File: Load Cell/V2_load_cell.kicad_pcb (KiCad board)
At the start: 2 copper layers, 114.3 x 114.3 mm, 35 parts, among them J1 Conn_01x02, J10 Conn_01x06, J11 Conn_01x04, J12 Conn_01x06, J13 Conn_01x04, J14 Conn_01x06, J15 Conn_01x04, J16 Conn_01x06, J17 Conn_01x04, J2 Conn_01x06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

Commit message: 2-17-22
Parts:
- moved A1 18.4 mm to (74.9, 31.8)
- moved J1 18.4 mm to (81.3, 19.1)
- moved R4 12.7 mm to (38.7, 30.5), turned to 0 degrees
- moved R2 12.7 mm to (18.4, 30.5), turned to 0 degrees
- moved R6 12.7 mm to (18.4, 74.3), turned to 0 degrees
- moved R8 12.7 mm to (37.5, 74.3), turned to 0 degrees
- moved R5 8.64 mm to (18.4, 78.7), turned to 0 degrees
- moved R7 8.64 mm to (37.5, 78.7), turned to 0 degrees
- moved R1 7.96 mm to (18.4, 34.9), turned to 0 degrees
- moved R3 7.96 mm to (38.7, 34.9), turned to 0 degrees
- moved J11 2.54 mm to (21.0, 66.7)
- moved J13 2.54 mm to (41.3, 66.7)
- moved J10 2.54 mm to (31.1, 41.3)
- moved J12 2.54 mm to (51.4, 41.3)
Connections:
- J10 pad 3: /A+0 -> /Sheet61D3CBFB/A-
- J10 pad 4: /Sheet61D3CBFB/A- -> /A+0
- J11 pad 1: VCC -> GND
- J11 pad 4: GND -> VCC
- J12 pad 3: /A+1 -> /sheet61D4E250/A-
- J12 pad 4: /sheet61D4E250/A- -> /A+1
- J13 pad 1: VCC -> GND
- J13 pad 4: GND -> VCC
- J14 pad 3: /A+2 -> /sheet61D4EE5D/A-
- J14 pad 4: /sheet61D4EE5D/A- -> /A+2
- J15 pad 1: VCC -> GND
- J15 pad 4: GND -> VCC
- J16 pad 3: /A+3 -> /sheet61D4FC90/A-
- J16 pad 4: /sheet61D4FC90/A- -> /A+3
- J17 pad 1: VCC -> GND
- J17 pad 4: GND -> VCC
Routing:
- net VCC: track 207.8 -> 159.5 mm
- net /DT2: track 71.3 -> 97.0 mm
- net /SCK2: track 67.0 -> 91.5 mm
- net /A+1: track 69.2 -> 93.6 mm
- net /DT0: track 44.1 -> 67.3 mm
- net /SCK0: track 40.6 -> 62.2 mm
- net /DT1: track 21.7 -> 42.6 mm
- net /SCK1: track 18.1 -> 37.9 mm
- net /DT3: track 55.8 -> 73.2 mm
- net /SCK3: track 51.4 -> 68.2 mm
- net /A1: track 60.5 -> 75.7 mm
- net /TX1: track 57.1 -> 71.6 mm
- net /A+0: track 23.6 -> 34.6 mm
- net /E+2: track 40.0 -> 50.5 mm
- net /E+3: track 79.9 -> 90.4 mm
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- added copper zone on B.Cu, net GND

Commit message: pcb v2 update
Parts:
- J6, J7, J8, J9: footprint Connector_JST:JST_PH_B3B-PH-K_1x03_P2.00mm_Vertical -> Connector_JST:JST_PH_S3B-PH-K_1x03_P2.00mm_Horizontal
- moved J6 6.04 mm to (33.8, 19.7), turned to 180 degrees
- moved J7 4.02 mm to (109.9, 19.7), turned to 180 degrees
- moved H2 1.91 mm to (120.7, 19.1)
- moved J9 1.46 mm to (105.9, 119.4)
- moved J8 0.63 mm to (29.8, 119.4)
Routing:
- net VCC: track 159.5 -> 239.2 mm
- net /A+1: track 93.6 -> 77.6 mm
- net /E+1: track 67.0 -> 77.5 mm
- net /A+0: track 34.6 -> 41.5 mm
- net /E-0: track 24.5 -> 27.8 mm
- net /VIN: track 28.7 -> 26.8 mm
- net /E+3: track 90.4 -> 88.7 mm
- net /E+0: track 27.8 -> 29.3 mm
- net /E-3: track 86.3 -> 85.5 mm
- net /E+2: track 50.5 -> 51.3 mm

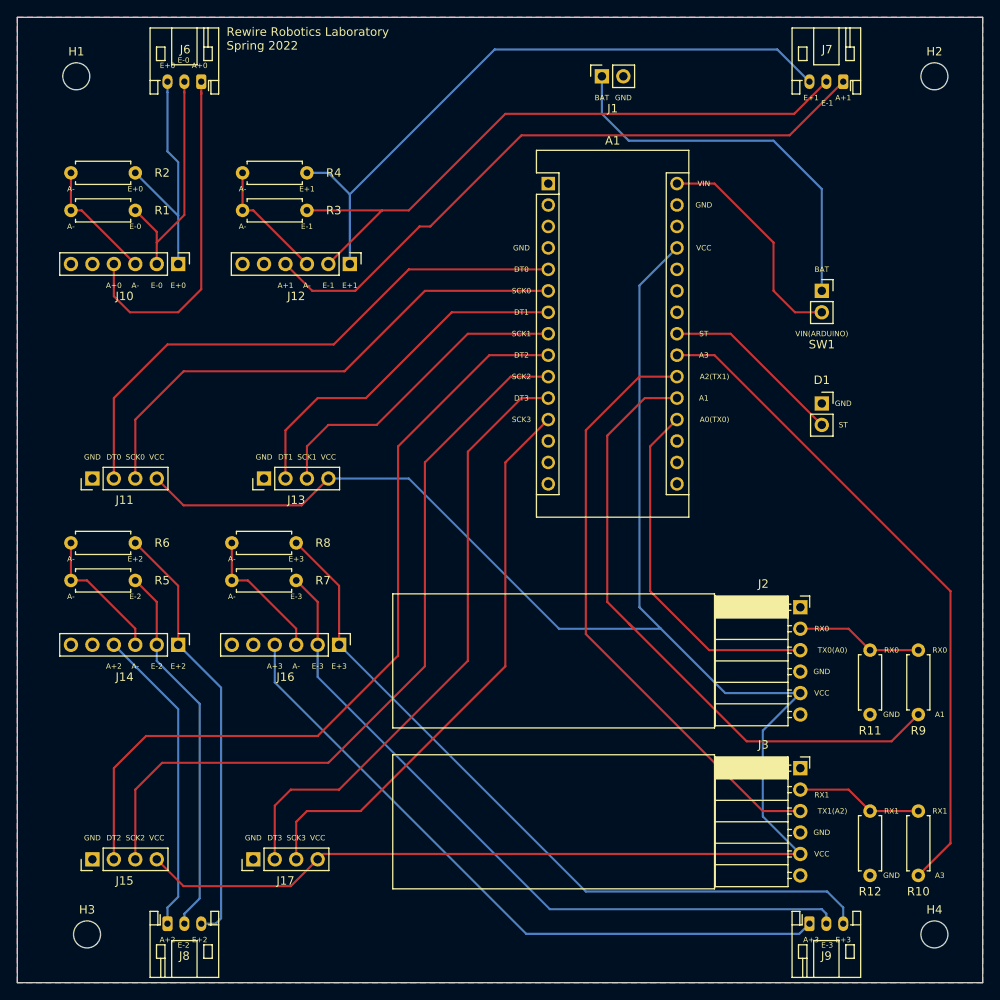
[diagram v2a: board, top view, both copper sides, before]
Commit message: JST connectors, increased track width of VCC, moved bluetooth modules, other small fixes
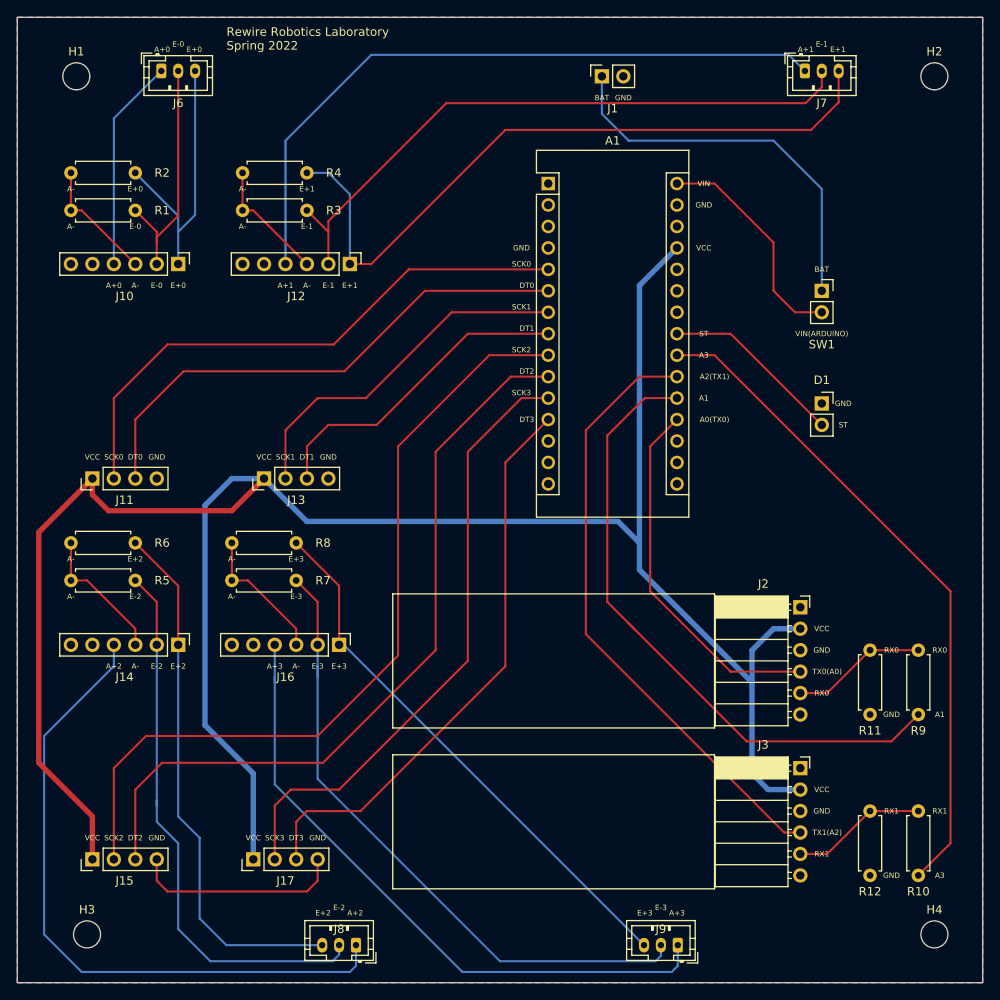
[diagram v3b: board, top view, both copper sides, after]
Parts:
- J6, J7, J8, J9: footprint Connector_JST:JST_PH_S3B-PH-K_1x03_P2.00mm_Horizontal -> Connector_JST:JST_PH_B3B-PH-K_1x03_P2.00mm_Vertical
- moved J8 22.5 mm to (52.2, 121.9), turned to 180 degrees
- moved J9 15.8 mm to (90.3, 121.9), turned to 180 degrees
- moved J6 4.90 mm to (29.1, 18.4), turned to 0 degrees
- moved J7 4.71 mm to (105.3, 18.4), turned to 0 degrees
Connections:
- A1 pad 10: /SCK2 -> /DT2
- A1 pad 11: /DT3 -> /SCK3
- A1 pad 12: /SCK3 -> /DT3
- A1 pad 5: /DT0 -> /SCK0
- A1 pad 6: /SCK0 -> /DT0
- A1 pad 7: /DT1 -> /SCK1
- A1 pad 8: /SCK1 -> /DT1
- A1 pad 9: /DT2 -> /SCK2
- J11 pad 1: GND -> VCC
- J11 pad 2: /DT0 -> /SCK0
- J11 pad 3: /SCK0 -> /DT0
- J11 pad 4: VCC -> GND
- J13 pad 1: GND -> VCC
- J13 pad 2: /DT1 -> /SCK1
- J13 pad 3: /SCK1 -> /DT1
- J13 pad 4: VCC -> GND
- J15 pad 1: GND -> VCC
- J15 pad 2: /DT2 -> /SCK2
- J15 pad 3: /SCK2 -> /DT2
- J15 pad 4: VCC -> GND
- J17 pad 1: GND -> VCC
- J17 pad 2: /DT3 -> /SCK3
- J17 pad 3: /SCK3 -> /DT3
- J17 pad 4: VCC -> GND
- J2 pad 2: /RX0 -> VCC
- J2 pad 3: /TX0 -> GND
- J2 pad 4: GND -> /TX0
- J2 pad 5: VCC -> /RX0
- J3 pad 2: /RX1 -> VCC
- J3 pad 3: /TX1 -> GND
- J3 pad 4: GND -> /TX1
- J3 pad 5: VCC -> /RX1
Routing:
- net /A+2: track 36.7 -> 79.2 mm
- net GND: track 0.00 -> 25.2 mm
- net /E+3: track 88.7 -> 65.0 mm
- net VCC: track 239.2 -> 261.8 mm
- net /E-2: track 44.5 -> 66.1 mm
- net /A+0: track 41.5 -> 25.8 mm
- net /E+2: track 51.3 -> 64.3 mm
- net /E-3: track 85.5 -> 76.9 mm
- net /E+1: track 77.5 -> 83.9 mm
- net /DT2: track 97.0 -> 91.2 mm
- net /SCK2: track 91.5 -> 97.0 mm
- net /SCK0: track 62.2 -> 67.3 mm
- net /DT0: track 67.3 -> 62.2 mm
- net /SCK3: track 68.2 -> 73.2 mm
- net /DT3: track 73.2 -> 68.2 mm
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
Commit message: commit
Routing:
- net /SCK0: track 67.3 -> 38.2 mm
- net /DT0: track 62.2 -> 34.1 mm
- net /SCK1: track 42.6 -> 16.8 mm
- net /DT1: track 37.9 -> 13.1 mm
- net /SCK2: track 97.0 -> 74.7 mm
- net /DT2: track 91.2 -> 74.1 mm
- net /SCK3: track 73.2 -> 61.1 mm
- net /DT3: track 68.2 -> 61.0 mm

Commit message: v2
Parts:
- J6, J7, J8, J9: moved to B.Cu
- moved A1 38.7 mm to (90.2, 67.3), turned to 180 degrees
- moved J6 4.00 mm to (33.1, 18.4), turned to 180 degrees
- moved J8 4.00 mm to (48.2, 121.9), turned to 0 degrees
- moved J9 4.00 mm to (86.3, 121.9), turned to 0 degrees
- moved J7 3.91 mm to (109.2, 18.4), turned to 180 degrees
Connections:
- A1 pad 10: /DT2 -> /DT0
- A1 pad 11: /SCK3 -> /SCK0
- A1 pad 12: /DT3 -> Net-(A1-Pad12)
- A1 pad 19: /TX0 -> /SCK1
- A1 pad 20: /A1 -> /DT1
- A1 pad 21: /TX1 -> /SCK2
- A1 pad 22: /A3 -> /DT2
- A1 pad 23: /ST -> /SCK3
- A1 pad 24: Net-(A1-Pad24) -> /DT3
- A1 pad 5: /SCK0 -> /ST
- A1 pad 6: /DT0 -> /A3
- A1 pad 7: /SCK1 -> /TX0
- A1 pad 8: /DT1 -> /A1
- A1 pad 9: /SCK2 -> /TX1
- J6 pad 1: /A+0 -> /E+0
- J6 pad 3: /E+0 -> /A+0
- J7 pad 1: /A+1 -> /E+1
- J7 pad 3: /E+1 -> /A+1
- J8 pad 1: /A+2 -> /E+2
- J8 pad 3: /E+2 -> /A+2
- J9 pad 1: /A+3 -> /E+3
- J9 pad 3: /E+3 -> /A+3
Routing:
- net /SCK0: track 38.2 -> 96.3 mm
- net /DT0: track 34.1 -> 91.0 mm
- net /VIN: track 26.8 -> 75.6 mm
- net /SCK1: track 16.8 -> 45.8 mm
- net /DT1: track 13.1 -> 41.1 mm
- net /SCK2: track 74.7 -> 102.3 mm
- net /DT2: track 74.1 -> 96.2 mm
- net VCC: track 261.8 -> 242.1 mm
- net /SCK3: track 61.1 -> 79.0 mm
- net /DT3: track 61.0 -> 76.4 mm
- net /A3: track 79.2 -> 91.5 mm
- net /TX0: track 43.4 -> 54.0 mm
- net /TX1: track 72.7 -> 81.1 mm
- net /A1: track 75.7 -> 83.7 mm
- net /ST: track 21.6 -> 18.5 mm

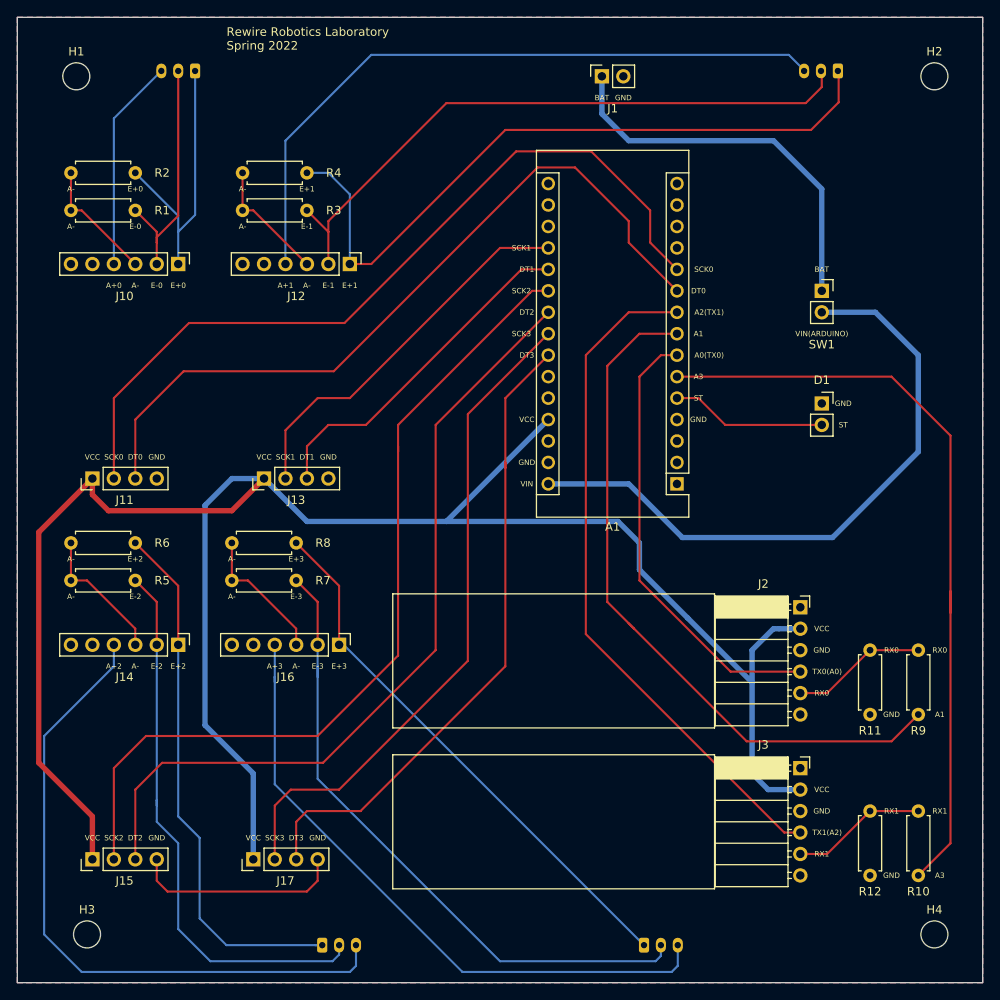
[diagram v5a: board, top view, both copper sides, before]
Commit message: Changes: - Moved mounting holes - Changed size of HC-05 footprint marker - Moved one trace in the bottom left corner - Redid STEP, Gerber, Drill files
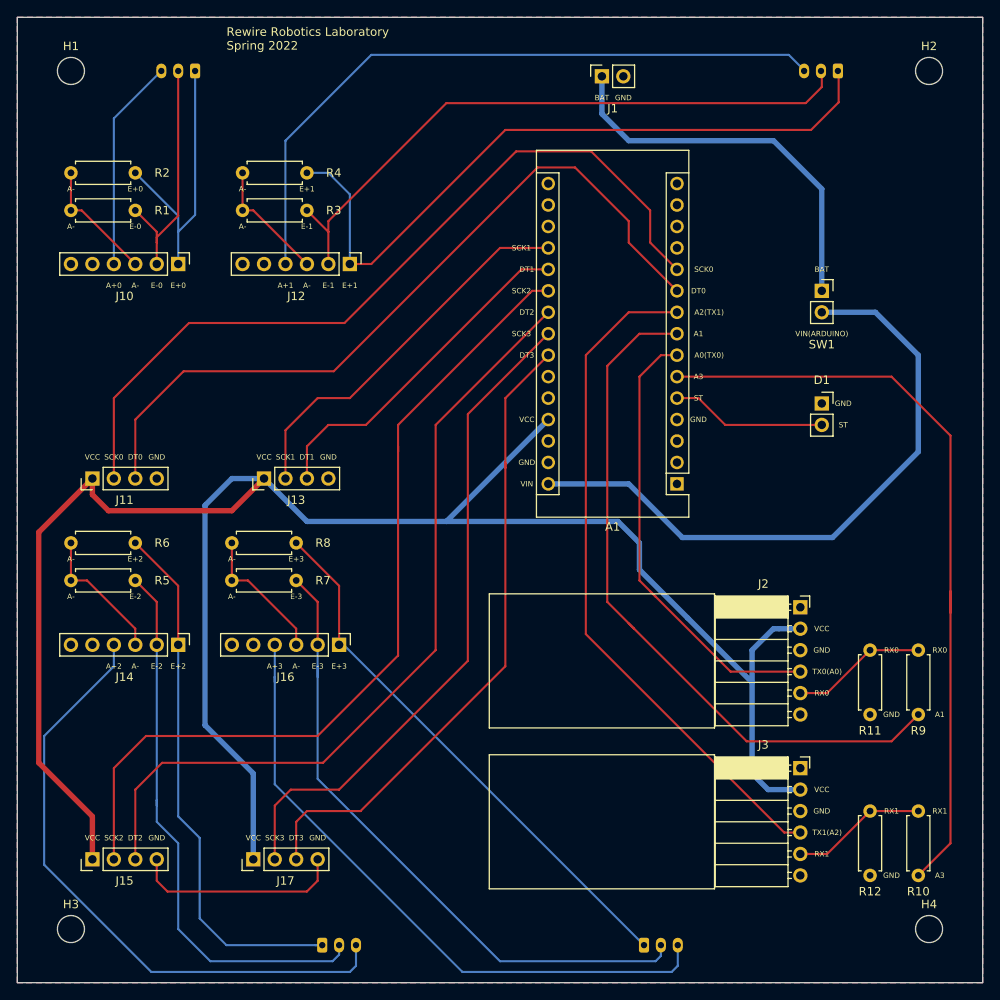
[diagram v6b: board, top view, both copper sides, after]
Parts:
- moved H3 2.01 mm to (18.4, 120.0)
- moved H4 0.90 mm to (120.0, 120.0)
- moved H2 0.90 mm to (120.0, 18.4)
- moved H1 0.90 mm to (18.4, 18.4)
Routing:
- net /A+2: track 79.2 -> 74.4 mm

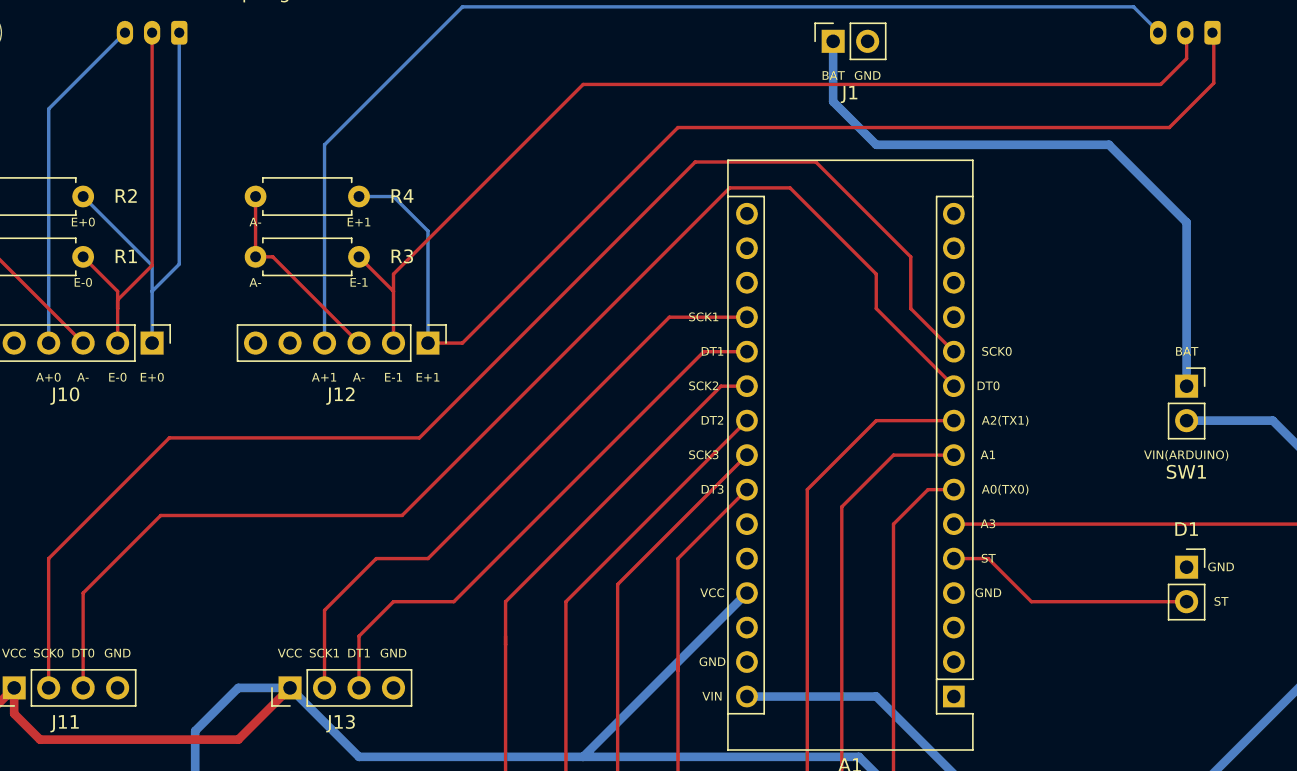
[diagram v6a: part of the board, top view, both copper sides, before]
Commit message: should have fixed some trace clearance issues
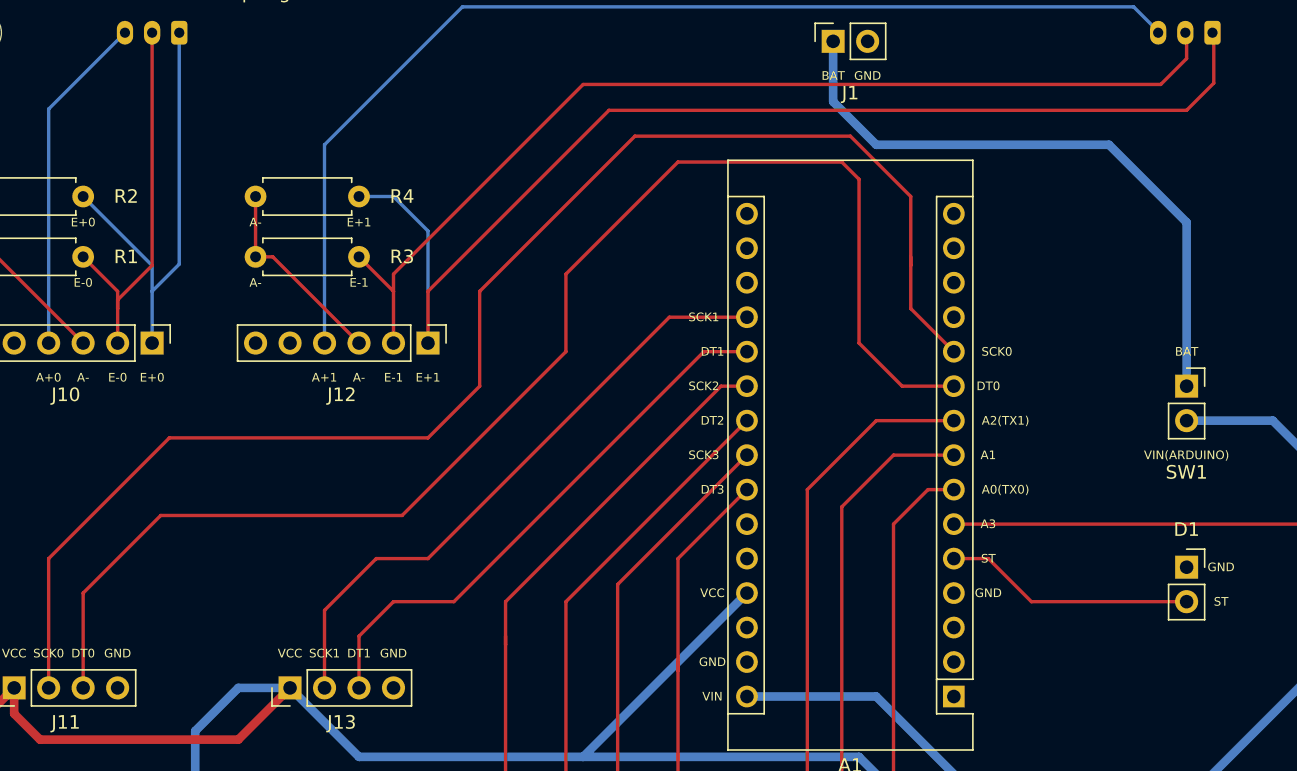
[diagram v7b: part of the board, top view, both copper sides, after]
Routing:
- net /DT0: track 91.0 -> 101.5 mm
- net /SCK0: track 96.3 -> 105.2 mm
- net /E+1: track 83.9 -> 86.1 mm
